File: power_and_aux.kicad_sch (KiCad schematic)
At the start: 28 parts, among them J2 GND, J3 Aux 5VDC, J5 Power 5V, J6 FTDI Serial2USB, SW1 Power SW, SW2 RESET, U4 74HCT00, U5 74LS30, U6 DS1813

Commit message: Schematic re-organized
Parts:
- added J4: Expansion Bus, Connector_PinSocket_2.54mm:PinSocket_2x20_P2.54mm_Vertical, symbol Connector_Generic:Conn_02x20_Odd_Even
- added JP2: CLK SEL, Connector_PinHeader_2.54mm:PinHeader_1x03_P2.54mm_Vertical, symbol Connector:Conn_01x03_Male
- added TP1: CLK, TestPoint:TestPoint_THTPad_1.0x1.0mm_Drill0.5mm, symbol Connector:TestPoint_Probe
- added TP2: RDY, TestPoint:TestPoint_THTPad_1.0x1.0mm_Drill0.5mm, symbol Connector:TestPoint_Probe
- added TP3: ACIA_CLK, TestPoint:TestPoint_THTPad_1.0x1.0mm_Drill0.5mm, symbol Connector:TestPoint_Probe
- added TP4: ~{ACIA_IRQ}, TestPoint:TestPoint_THTPad_1.0x1.0mm_Drill0.5mm, symbol Connector:TestPoint_Probe
- added TP5: ~{IRQ}, TestPoint:TestPoint_THTPad_1.0x1.0mm_Drill0.5mm, symbol Connector:TestPoint_Probe
- added X1: OSC, Oscillator:Oscillator_DIP-14, symbol Oscillator:CXO_DIP14
- TP6: renamed from TP4; footprint TestPoint:TestPoint_THTPad_1.5x1.5mm_Drill0.7mm -> TestPoint:TestPoint_THTPad_1.0x1.0mm_Drill0.5mm
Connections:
- net +5V: now also J4.2 (Pin_2), J4.39 (Pin_39), X1.14 (Vcc)
- net GND: now also J4.1 (Pin_1), J4.40 (Pin_40), JP2.1 (Pin_1), X1.7 (GND)
- net ~{RESET}: now also J4.28 (Pin_28)
- new net ACIA_CLK: TP3.1
- new net CLK: J4.29 (Pin_29), JP2.2 (Pin_2), TP1.1
- new net OSC_OUT: JP2.3 (Pin_3), X1.8 (OUT)
- new net RDY: TP2.1
- new net R~{W}: J4.27 (Pin_27)
- new net a0: J4.11 (Pin_11)
- new net a1: J4.12 (Pin_12)
- new net a10: J4.21 (Pin_21)
- new net a11: J4.22 (Pin_22)
- new net a12: J4.23 (Pin_23)
- new net a13: J4.24 (Pin_24)
- new net a14: J4.25 (Pin_25)
- new net a15: J4.26 (Pin_26)
- new net a2: J4.13 (Pin_13)
- new net a3: J4.14 (Pin_14)
- new net a4: J4.15 (Pin_15)
- new net a5: J4.16 (Pin_16)
- new net a6: J4.17 (Pin_17)
- new net a7: J4.18 (Pin_18)
- new net a8: J4.19 (Pin_19)
- new net a9: J4.20 (Pin_20)
- new net d0: J4.3 (Pin_3)
- new net d1: J4.4 (Pin_4)
- new net d2: J4.5 (Pin_5)
- new net d3: J4.6 (Pin_6)
- new net d4: J4.7 (Pin_7)
- new net d5: J4.8 (Pin_8)
- new net d6: J4.9 (Pin_9)
- new net d7: J4.10 (Pin_10)
- new net ~{ACIA_IRQ}: TP4.1
- new net ~{IO_3}: J4.31 (Pin_31)
- new net ~{IO_4}: J4.33 (Pin_33)
- new net ~{IO_5}: J4.35 (Pin_35)
- new net ~{IO_6}: J4.37 (Pin_37)
- new net ~{IO_7}: J4.38 (Pin_38)
- new net ~{IO_8}: J4.36 (Pin_36)
- new net ~{IO_CS}: J4.34 (Pin_34)
- new net ~{IRQ}: J4.30 (Pin_30), TP5.1
- new net ~{NMI}: J4.32 (Pin_32)
- no-connect marks 0 -> 1
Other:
- note added: "Clock"
- note added: "Expansion Bus"
- note added: "Mounting Holes"
- note added: "Testing Points"
- company: (none) -> (c) Mariano Luna
- title: (none) -> YAsixfive02 SBC
- moved on the sheet: J6, R10, R7, R8, R9, SW2, TP6, U6

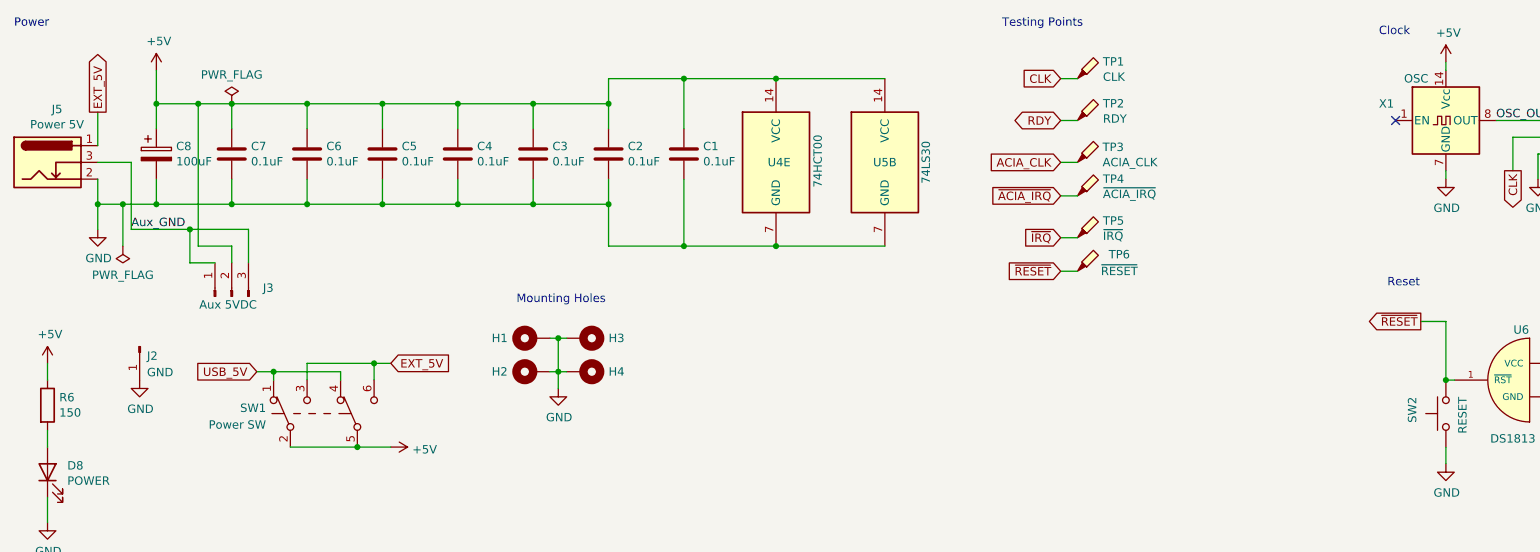
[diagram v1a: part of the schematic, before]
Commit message: Schematic and PCB Updated
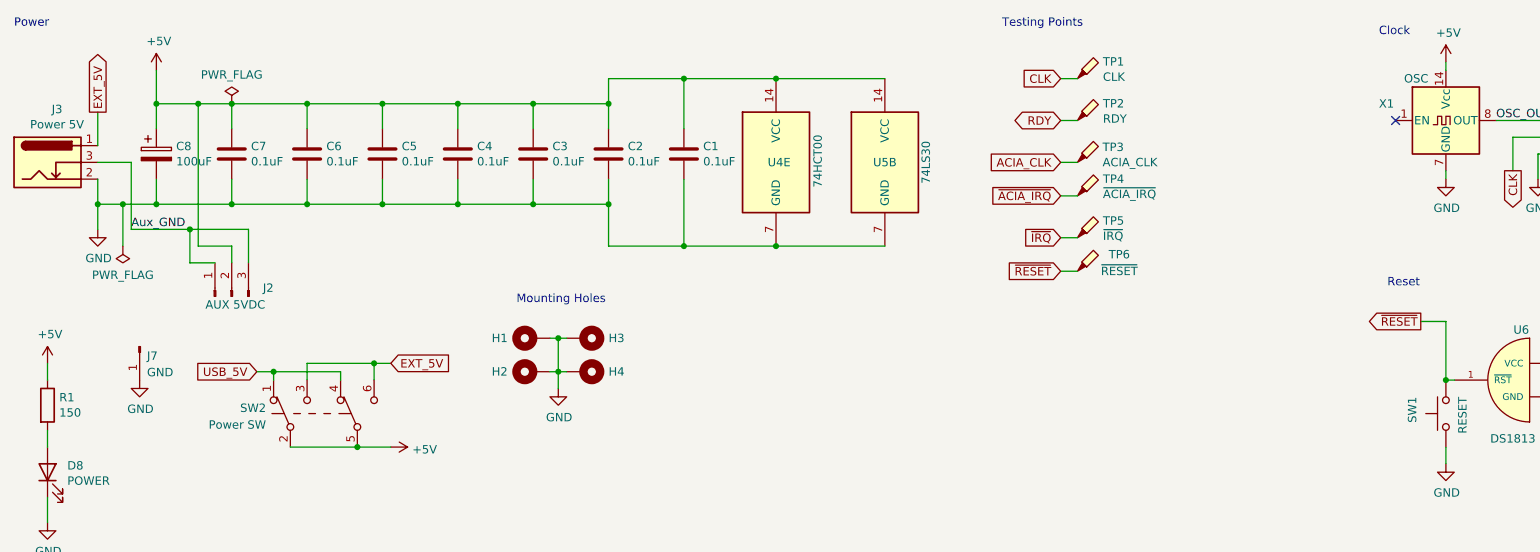
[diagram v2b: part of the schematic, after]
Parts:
- J2: renamed from J3; value Aux 5VDC -> AUX 5VDC
- renumbered J5 to J3, J2 to J7, R6 to R1, SW2 to SW1, SW1 to SW2
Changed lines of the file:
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@@
   (symbol (lib_id "Switch:SW_Push_DPDT") (at 64.77 76.2 90) (unit 1)
     (in_bom yes) (on_board yes) (fields_autoplaced)
-    (property "Reference" "SW1" (id 0) (at 56.007 75.3653 90)
-      (effects (font (size 1.27 1.27)) (justify left))
-    )
-    (property "Value" "Power SW" (id 1) (at 56.007 77.9022 90)
+    (property "Reference" "SW2" (id 0) (at 56.0071 75.3653 90)
+      (effects (font (size 1.27 1.27)) (justify left))
+    )
+    (property "Value" "Power SW" (id 1) (at 56.0071 77.9022 90)
       (effects (font (size 1.27 1.27)) (justify left))
     )
@@
   (symbol (lib_id "Connector:Conn_01x03_Male") (at 50.8 58.42 90) (unit 1)
     (in_bom yes) (on_board yes)
-    (property "Reference" "J3" (id 0) (at 57.15 57.15 90)
-      (effects (font (size 1.27 1.27)) (justify left))
-    )
-    (property "Value" "Aux 5VDC" (id 1) (at 54.61 59.69 90)
+    (property "Reference" "J2" (id 0) (at 57.15 57.15 90)
+      (effects (font (size 1.27 1.27)) (justify left))
+    )
+    (property "Value" "AUX 5VDC" (id 1) (at 55.88 59.69 90)
       (effects (font (size 1.27 1.27)) (justify left))
     )
@@
   (symbol (lib_id "Connector:Conn_01x01_Male") (at 36.83 66.04 270) (unit 1)
     (in_bom yes) (on_board yes)
-    (property "Reference" "J2" (id 0) (at 37.9476 67.4624 90)
+    (property "Reference" "J7" (id 0) (at 37.9476 67.4624 90)
       (effects (font (size 1.27 1.27)) (justify left))
     )
@@
   (symbol (lib_id "Switch:SW_Push") (at 234.95 76.2 90) (unit 1)
     (in_bom yes) (on_board yes)
-    (property "Reference" "SW2" (id 0) (at 229.87 73.66 0)
+    (property "Reference" "SW1" (id 0) (at 229.87 73.66 0)
       (effects (font (size 1.27 1.27)) (justify right))
     )
@@
   (symbol (lib_id "Connector:Barrel_Jack_Switch") (at 22.86 38.1 0) (unit 1)
     (in_bom yes) (on_board yes)
-    (property "Reference" "J5" (id 0) (at 24.3078 30.0482 0))
+    (property "Reference" "J3" (id 0) (at 24.3078 30.0482 0))
     (property "Value" "Power 5V" (id 1) (at 24.3078 32.3596 0))
     (property "Footprint" "Connector_BarrelJack:BarrelJack_Horizontal" (id 2) (at 24.13 39.116 0)
@@
   (symbol (lib_id "Device:R") (at 22.86 74.93 0) (unit 1)
     (in_bom yes) (on_board yes)
-    (property "Reference" "R6" (id 0) (at 24.638 73.7616 0)
-      (effects (font (size 1.27 1.27)) (justify left))
-    )
+    (property "Reference" "R1" (id 0) (at 24.638 73.7616 0)
+      (effects (font (size 1.27 1.27)) (justify left))
+    )

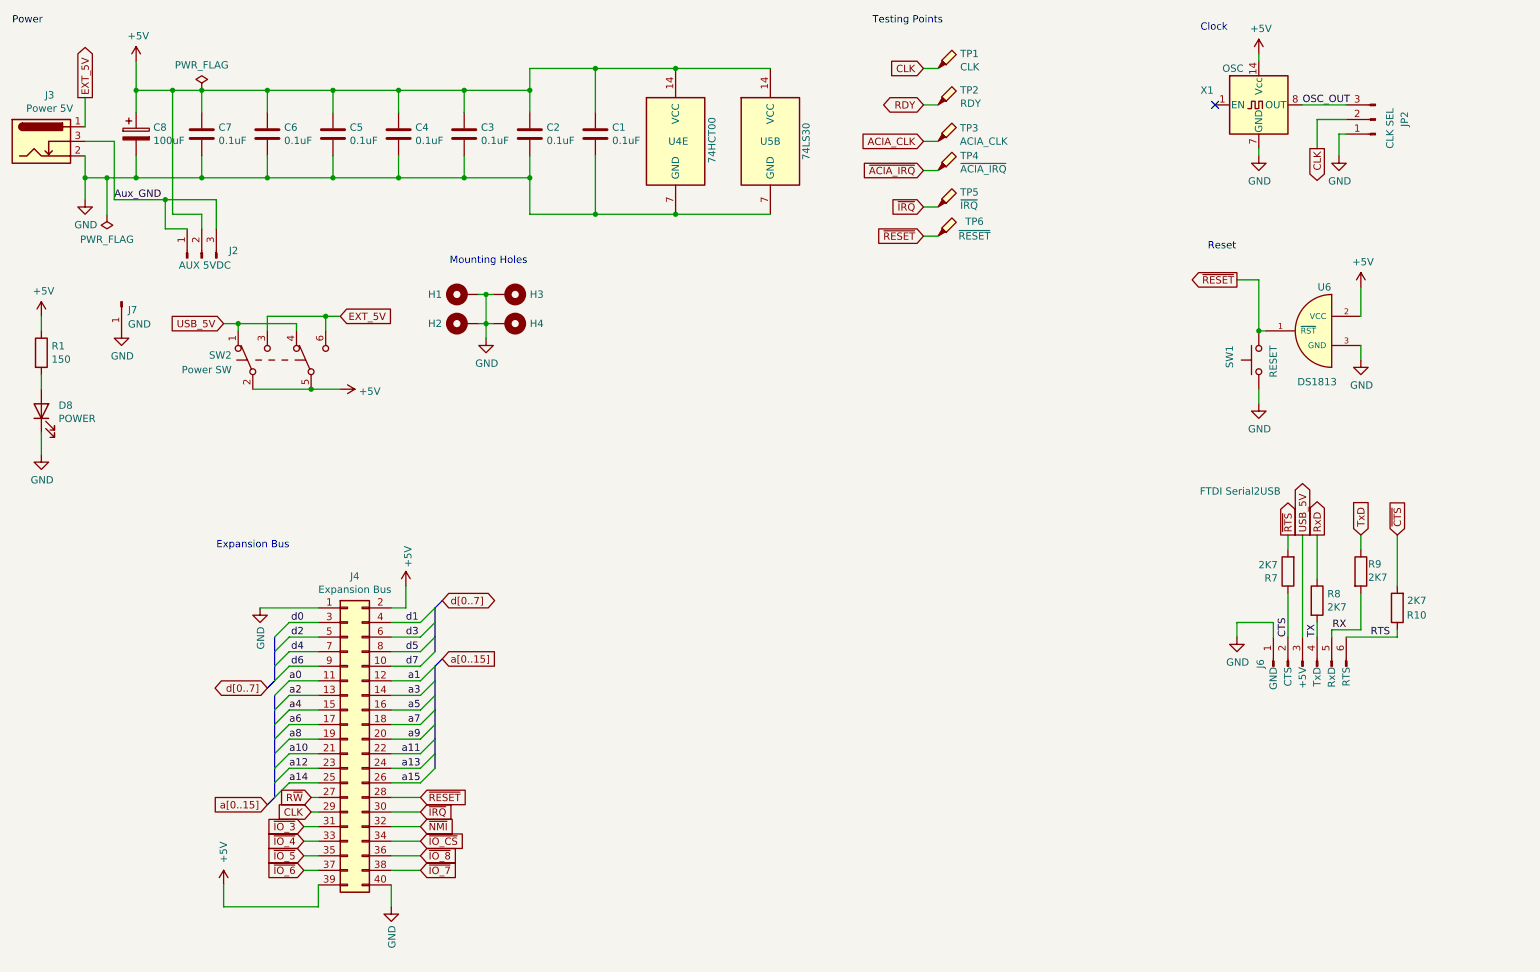
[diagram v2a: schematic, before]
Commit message: Added 6502 bus to schematic
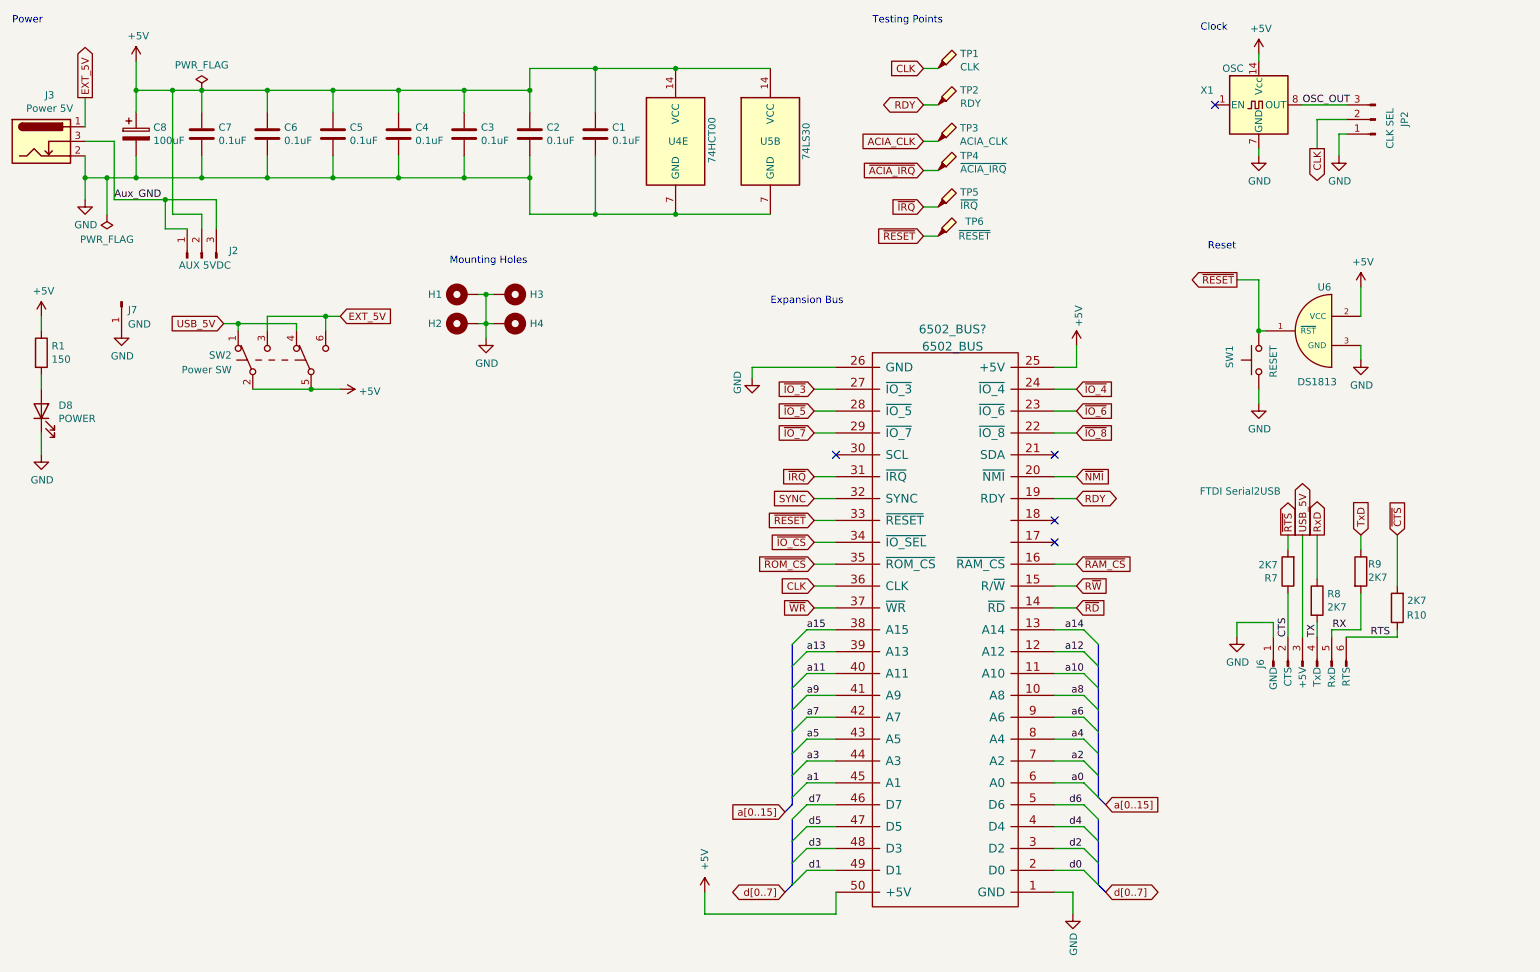
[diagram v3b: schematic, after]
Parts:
- removed J4: Expansion Bus, Connector_PinSocket_2.54mm:PinSocket_2x20_P2.54mm_Vertical, symbol Connector_Generic:Conn_02x20_Odd_Even
- added 6502_BUS?: 6502_BUS, symbol 6502_Bus:6502_BUS
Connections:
- net +5V: now also 6502_BUS?.25 (+5V), 6502_BUS?.50 (+5V)
- net CLK: now also 6502_BUS?.36 (CLK)
- net GND: now also 6502_BUS?.1 (GND), 6502_BUS?.26 (GND)
- net RDY: now also 6502_BUS?.19 (RDY)
- net R~{W}: now also 6502_BUS?.15 (R/~{W})
- net a0: now also 6502_BUS?.6 (A0)
- net a1: now also 6502_BUS?.45 (A1)
- net a10: now also 6502_BUS?.11 (A10)
- net a11: now also 6502_BUS?.40 (A11)
- net a12: now also 6502_BUS?.12 (A12)
- net a13: now also 6502_BUS?.39 (A13)
- net a14: now also 6502_BUS?.13 (A14)
- net a15: now also 6502_BUS?.38 (A15)
- net a2: now also 6502_BUS?.7 (A2)
- net a3: now also 6502_BUS?.44 (A3)
- net a4: now also 6502_BUS?.8 (A4)
- net a5: now also 6502_BUS?.43 (A5)
- net a6: now also 6502_BUS?.9 (A6)
- net a7: now also 6502_BUS?.42 (A7)
- net a8: now also 6502_BUS?.10 (A8)
- net a9: now also 6502_BUS?.41 (A9)
- net d0: now also 6502_BUS?.2 (D0)
- net d1: now also 6502_BUS?.49 (D1)
- net d2: now also 6502_BUS?.3 (D2)
- net d3: now also 6502_BUS?.48 (D3)
- net d4: now also 6502_BUS?.4 (D4)
- net d5: now also 6502_BUS?.47 (D5)
- net d6: now also 6502_BUS?.5 (D6)
- net d7: now also 6502_BUS?.46 (D7)
- net ~{IO_3}: now also 6502_BUS?.27 (~{IO_3})
- net ~{IO_4}: now also 6502_BUS?.24 (~{IO_4})
- net ~{IO_5}: now also 6502_BUS?.28 (~{IO_5})
- net ~{IO_6}: now also 6502_BUS?.23 (~{IO_6})
- net ~{IO_7}: now also 6502_BUS?.29 (~{IO_7})
- net ~{IO_8}: now also 6502_BUS?.22 (~{IO_8})
- net ~{IO_CS}: now also 6502_BUS?.34 (~{IO_SEL})
- net ~{IRQ}: now also 6502_BUS?.31 (~{IRQ})
- net ~{NMI}: now also 6502_BUS?.20 (~{NMI})
- net ~{RESET}: now also 6502_BUS?.33 (~{RESET})
- new net SYNC: 6502_BUS?.32 (SYNC)
- new net ~{RAM_CS}: 6502_BUS?.16 (~{RAM_CS})
- new net ~{RD}: 6502_BUS?.14 (~{RD})
- new net ~{ROM_CS}: 6502_BUS?.35 (~{ROM_CS})
- new net ~{WR}: 6502_BUS?.37 (~{WR})
- no-connect marks 1 -> 5

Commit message: 6502 Bus Edge Connector done
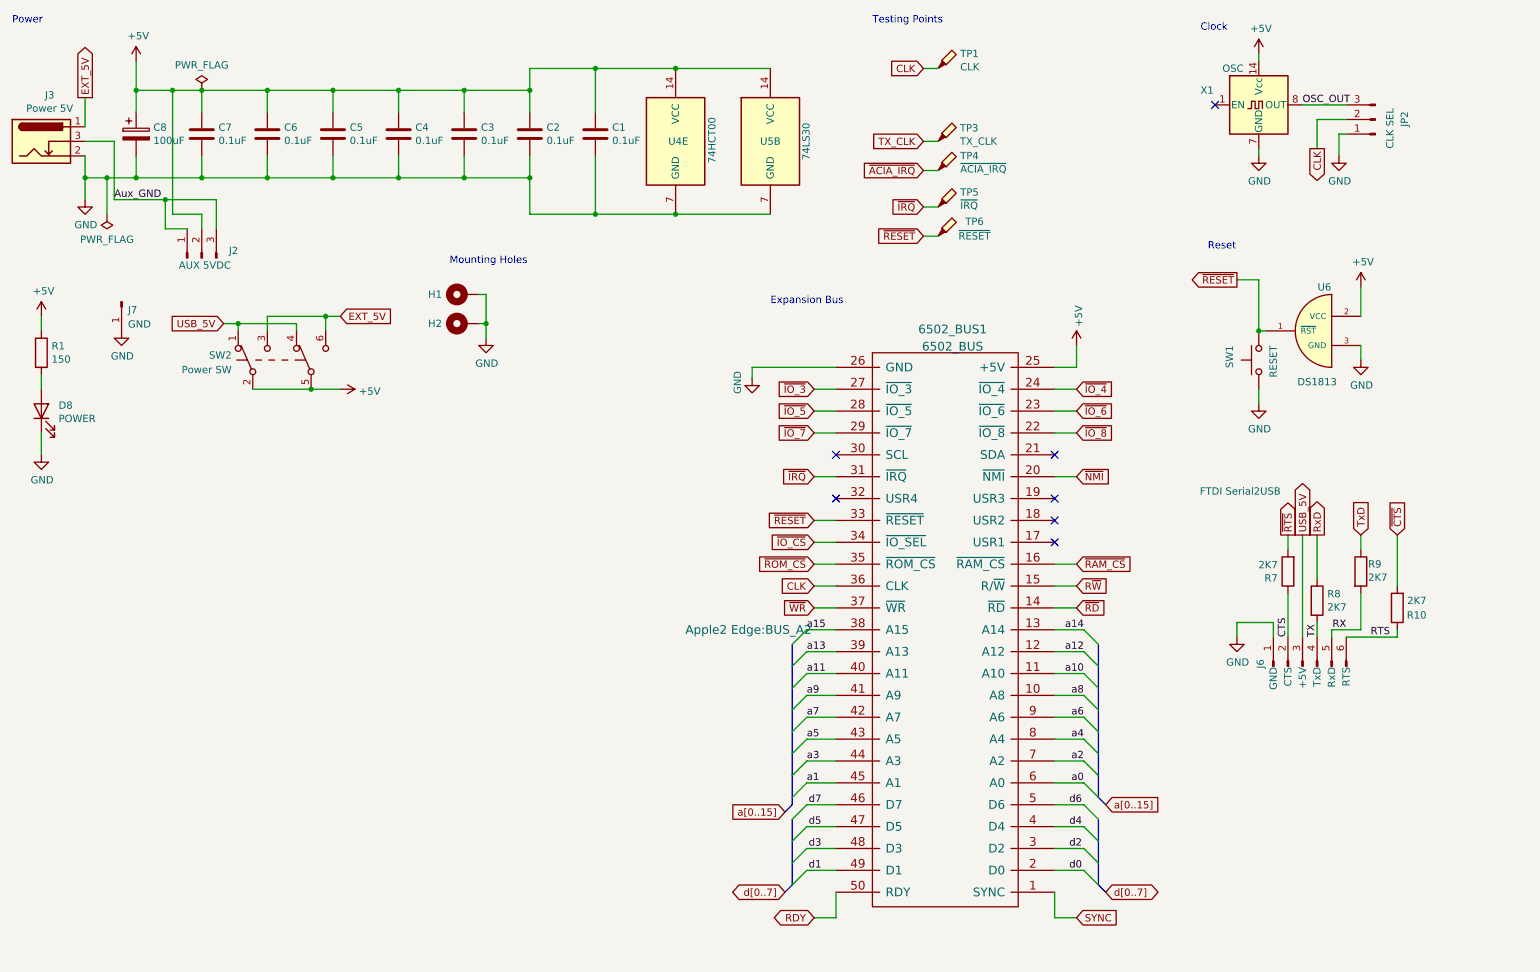
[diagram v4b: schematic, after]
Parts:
- removed H3, H4: MNT, MountingHole:MountingHole_3.2mm_M3_DIN965_Pad_TopBottom, symbol Mechanical:MountingHole_Pad
- removed TP2: RDY, TestPoint:TestPoint_THTPad_1.0x1.0mm_Drill0.5mm, symbol Connector:TestPoint_Probe
- 6502_BUS1: renamed from 6502_BUS?; footprint (none) -> Apple2 Edge:BUS_A2
- TP3: value ACIA_CLK -> TX_CLK
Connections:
- net +5V: no longer 6502_BUS1.50 (+5V)
- net GND: no longer 6502_BUS1.1 (GND)
- net RDY: now also 6502_BUS1.50 (RDY); no longer 6502_BUS1.19 (RDY)
- net SYNC: now also 6502_BUS1.1 (SYNC); no longer 6502_BUS1.32 (SYNC)
- net ACIA_CLK renamed TX_CLK
- no-connect marks 5 -> 7
